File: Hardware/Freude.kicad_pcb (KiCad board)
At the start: 4 copper layers, 10 parts, among them U1 IQS572

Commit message: Add uc, inter connects, futter to schematic
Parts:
- added REF**: Touchpad, Custom_Touchpad:Touchpad, B.Cu at (199.5, 75.8)
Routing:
- net (no net): track 0.00 -> 4.75 mm, vias 0 -> 1

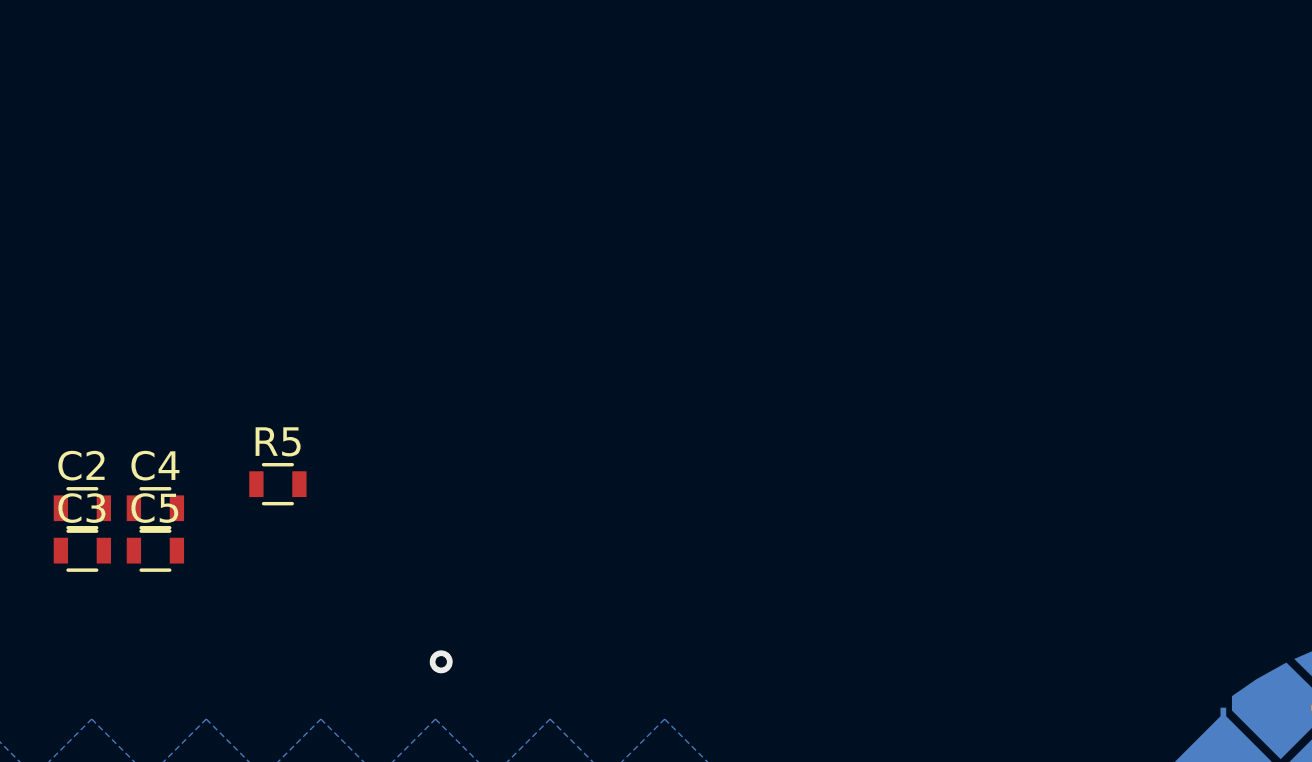
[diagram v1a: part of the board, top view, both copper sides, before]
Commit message: added 5 pin connector, added envelope for uc board, changed uc to low power smaller footprint after seeing envelope
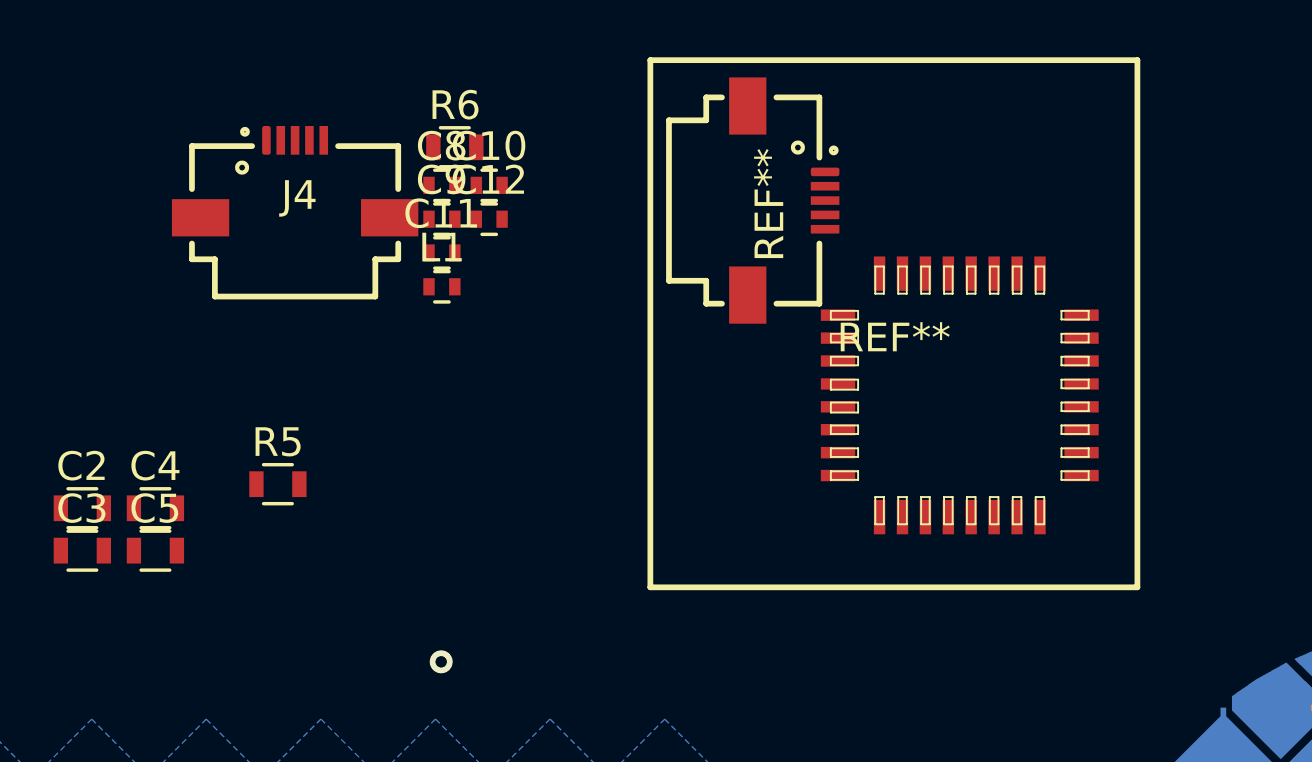
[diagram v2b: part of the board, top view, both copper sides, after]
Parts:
- added >NAME: >VALUE, SparkFun-DigitalIC:LQFP-32, F.Cu at (182.3, 54.9)
- added C10: 100pF, Resistors_SMD:R_0402, F.Cu at (165.9, 47.6)
- added C11: 100pF, Resistors_SMD:R_0402, F.Cu at (164.2, 49.9)
- added C12: 1uF, Resistors_SMD:R_0402, F.Cu at (165.9, 48.8)
- added C8: 100pF, Resistors_SMD:R_0402, F.Cu at (164.2, 47.6)
- added C9: 1uF, Resistors_SMD:R_0402, F.Cu at (164.2, 48.8)
- added J4: Conn_01x05_Female, .pretty:5051100592, F.Cu at (159.1, 46.0)
- added L1: Ferrite_Bead_Small, Resistors_SMD:R_0402, F.Cu at (164.2, 51.1)
- added R6: 0, Resistors_SMD:R_0603, F.Cu at (164.7, 46.2)
- added REF**: Joystick Envelope, .pretty:Joystick Envelope, F.Cu at (180.0, 52.4)
- added REF**: 5051100592, .pretty:5051100592, F.Cu at (177.6, 48.1)
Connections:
- net +3V3 renamed +3.3VA
- net /RDY renamed /RDY_TP
- net /SCL renamed /SCL_TP
- net /SDA renamed /SDA_TP
- C2 pad 1: Net-(C2-Pad1) -> GNDA
- C3 pad 1: Net-(C2-Pad1) -> GNDA
- C4 pad 1: Net-(C2-Pad1) -> GNDA
- C5 pad 1: Net-(C2-Pad1) -> GNDA
- R3 pad 2: GND -> GNDA
- R4 pad 2: GND -> GNDA
- R5 pad 2: GND -> GNDA
- U1 pad 5: GND -> GNDA

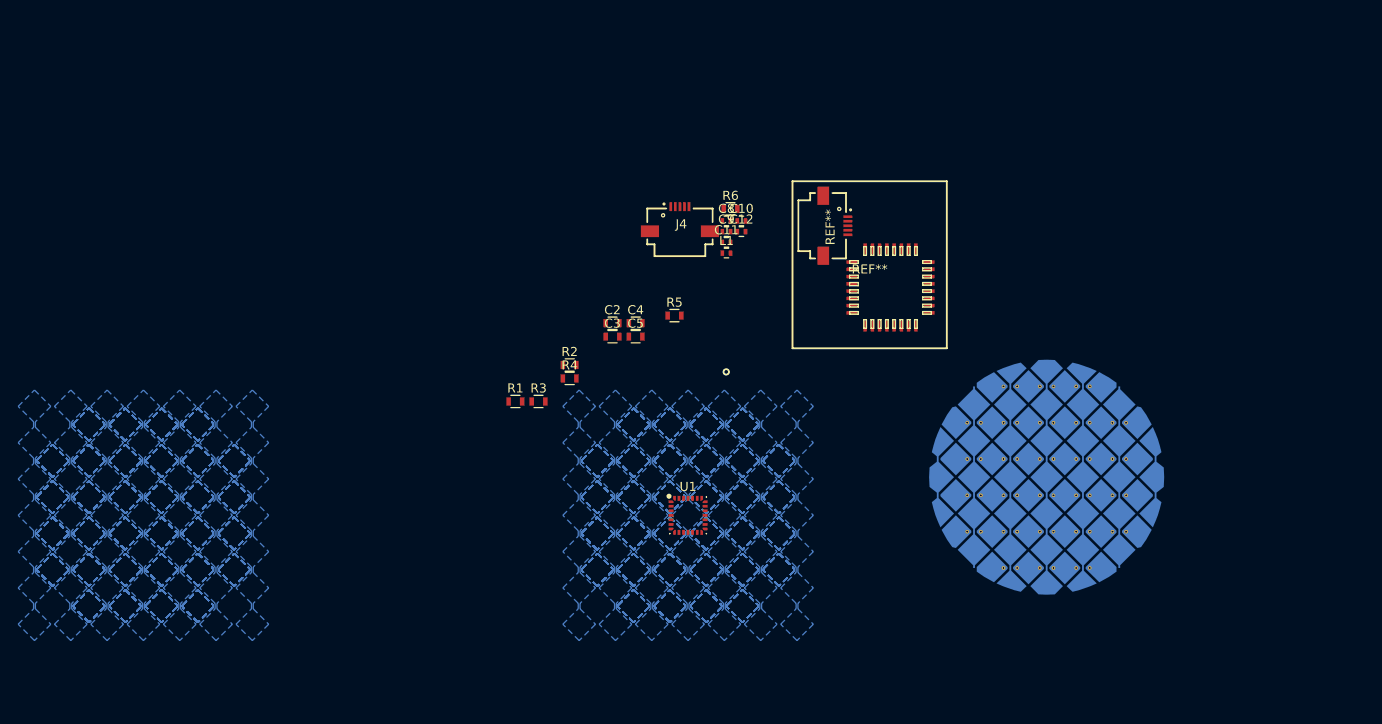
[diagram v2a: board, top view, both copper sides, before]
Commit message: add connectors, symbol for touch pad, start placement of touch controller
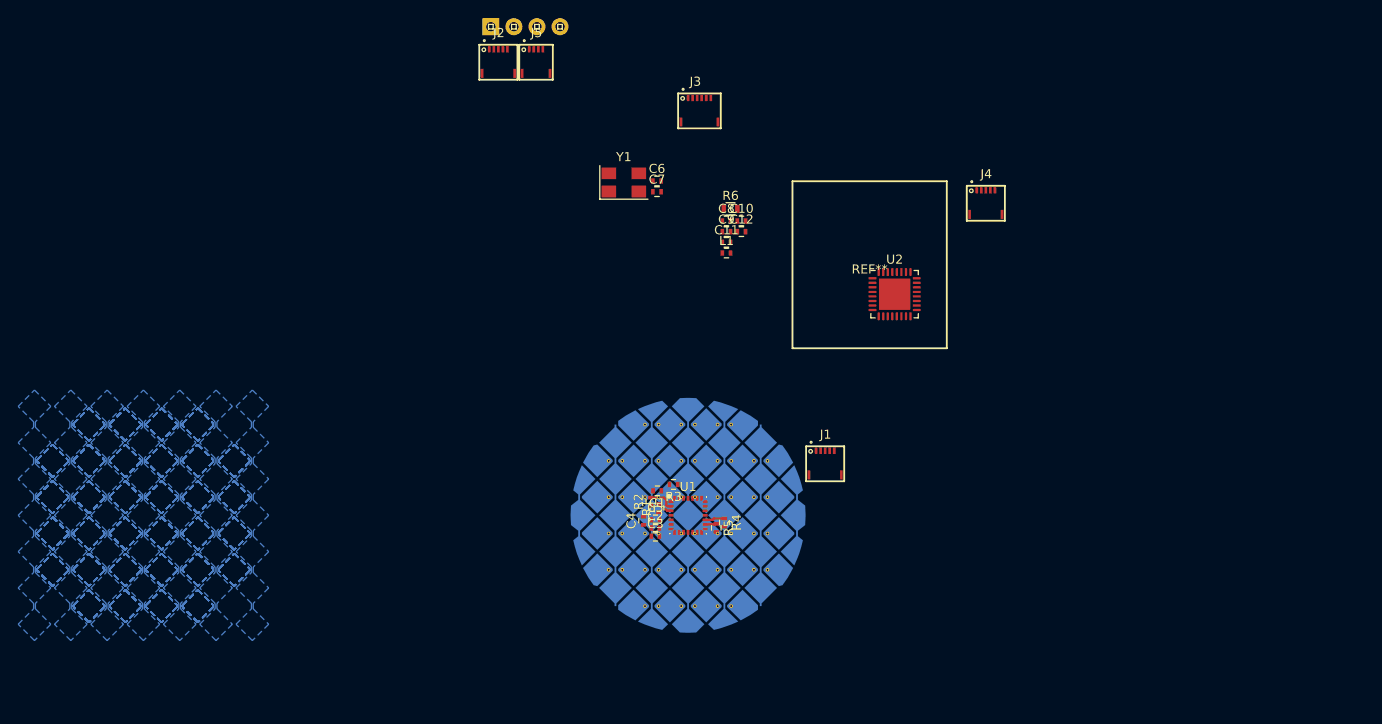
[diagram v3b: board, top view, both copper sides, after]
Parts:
- removed >NAME: >VALUE, SparkFun-DigitalIC:LQFP-32
- removed the REF** at (177.6, 48.1)
- added C1: C_Small, Resistors_SMD:R_0402, F.Cu at (156.6, 77.3)
- added C6: 30pF, Resistors_SMD:R_0402, F.Cu at (156.6, 43.2)
- added C7: 30pF, Resistors_SMD:R_0402, F.Cu at (156.6, 44.4)
- added J1: Conn_01x05_Female, .pretty:503480-0500, F.Cu at (175.1, 72.9)
- added J2: Conn_01x05_Female, .pretty:503480-0500, F.Cu at (139.1, 28.7)
- added J3: Conn_01x06_Female, .pretty:503480-0600, F.Cu at (161.3, 34.0)
- added J5: Conn_01x04_Female, .pretty:503480-0400, F.Cu at (143.3, 28.7)
- added J6: Conn_01x04_Male, SparkFun-Connectors:1X04, F.Cu at (138.3, 26.2)
- added U2: STM32L432KBUx, Package_DFN_QFN:QFN-32-1EP_5x5mm_P0.5mm_EP3.45x3.45mm, F.Cu at (182.8, 55.6)
- added Y1: Crystal_GND24, Crystal_SMD_5032-4pin_5.0x3.2mm, F.Cu at (152.9, 43.3)
- C2, C3, C4, C5, R1, R2, R3, R4, R5: footprint Resistors_SMD:R_0603 -> Resistors_SMD:R_0402
- J4: value Conn_01x05_Female -> Conn_01x04_Female; footprint .pretty:5051100592 -> .pretty:503480-0500
- moved REF** 39.7 mm to (160.0, 80.0)
- moved J4 33.7 mm to (192.8, 44.2)
- moved R5 23.8 mm to (163.1, 81.4), turned to 270 degrees
- moved R4 23.3 mm to (164.0, 80.8), turned to 270 degrees
- moved C2 23.0 mm to (156.4, 81.4)
- moved C3 22.5 mm to (156.4, 82.3)
- moved C4 21.8 mm to (155.1, 80.6), turned to 90 degrees
- moved C5 20.3 mm to (156.4, 80.5)
- moved R1 19.7 mm to (156.8, 79.2), turned to 90 degrees
- moved R2 17.5 mm to (155.9, 78.5), turned to 90 degrees
- moved R3 17.5 mm to (158.4, 76.6), turned to 180 degrees
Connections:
- J4 pad 2: GND -> /SWDIO
- J4 pad 3: /Switch_Out -> /SWCLK
- J4 pad 4: /DAC2_OUT1 -> GND
- J4 pad 5: +3V3 -> (no net)
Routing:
- net /SDA_TP: track 0.00 -> 2.67 mm
- net Net-(R4-Pad1): track 0.00 -> 2.19 mm
- net Net-(R5-Pad1): track 0.00 -> 1.25 mm
- net /SCL_TP: track 0.00 -> 0.71 mm
- net (no net): vias 1 -> 0

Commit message: Route touchpad complete *airhorn*, add switch schematic, add domain boxes schematic
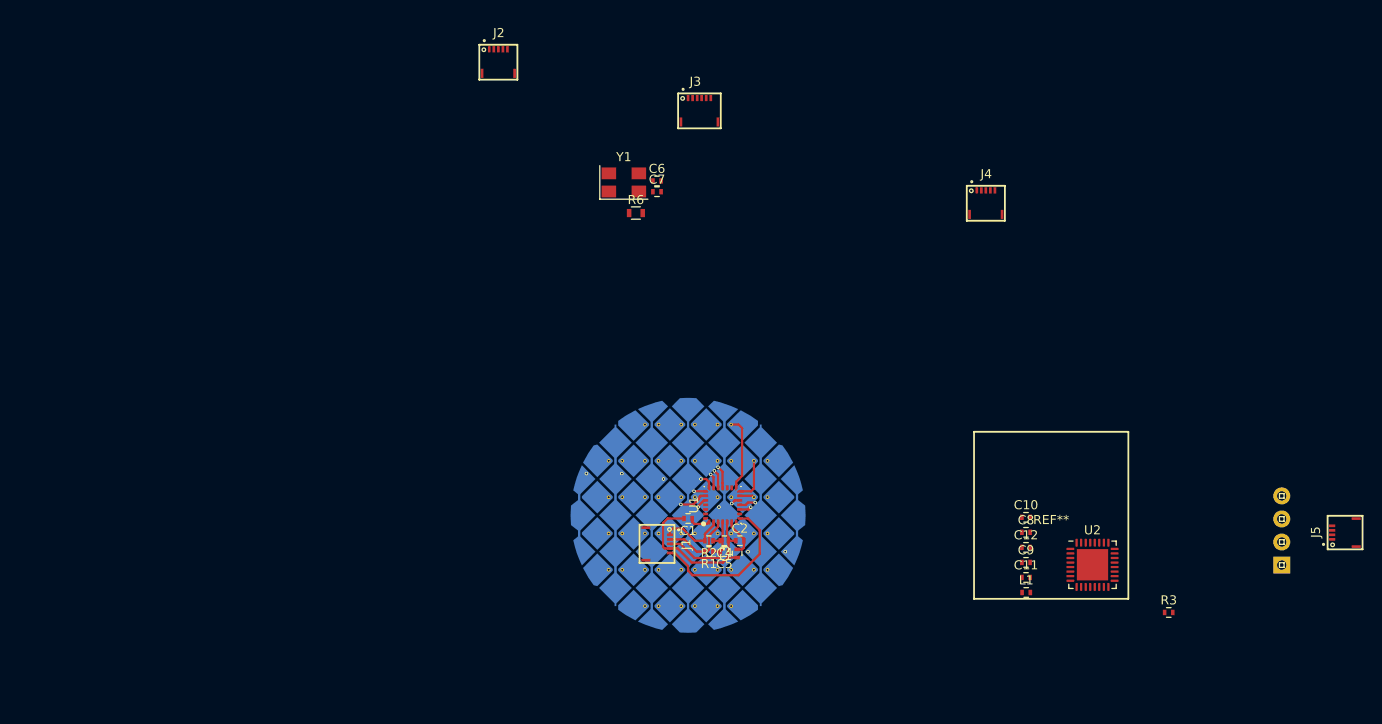
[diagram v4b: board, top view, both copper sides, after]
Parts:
- removed R4, R5: 0, Resistors_SMD:R_0402
- removed the REF** at (160.0, 80.0)
- added X1: Custom_Touchpad, Custom_Touchpad:Touchpad, B.Cu at (160.0, 80.0)
- R3: value 0 -> 10k
- moved J6 105.4 mm to (225.4, 85.5), turned to 90 degrees
- moved J5 102.6 mm to (230.9, 81.9), turned to 90 degrees
- moved R3 56.3 mm to (212.9, 90.7), turned to 0 degrees
- moved L1 49.9 mm to (197.2, 88.5)
- moved C11 49.5 mm to (197.2, 86.8)
- moved C9 49.2 mm to (197.2, 85.2)
- moved C8 47.6 mm to (197.2, 81.9)
- moved C12 46.8 mm to (197.2, 83.5)
- moved C10 45.3 mm to (197.2, 80.2)
- moved U2 36.9 mm to (204.6, 85.5)
- moved REF** 34.1 mm to (200.0, 80.0)
- moved J1 19.9 mm to (158.0, 83.2), turned to 270 degrees
- moved R6 10.4 mm to (154.2, 46.7)
- moved C2 9.40 mm to (165.7, 82.8)
- moved C3 9.20 mm to (165.4, 84.2), turned to 90 degrees
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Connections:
- net /VCC renamed /Prog_VCC
- net XA07 renamed Net-(U1-Pad25)
- J1 pad 1: +3.3VA -> /SDA_TP
- J1 pad 2: /SDA_TP -> /SCL_TP
- J1 pad 3: /SCL_TP -> +3.3VA
- J1 pad 4: /RDY_TP -> GNDA
- J1 pad 5: GNDA -> /RDY_TP
- J3 pad 1: +3V3 -> /SDA_UC
- J3 pad 2: /SDA_UC -> /SCL_UC
- J3 pad 3: /SCL_UC -> +3V3
- J3 pad 4: /RDY_UC -> GND
- J3 pad 5: GND -> /RDY_UC
- J5 pad 2: /SWDIO -> /Prog_SWDIO
- J5 pad 3: /SWCLK -> /Prog_SWCLK
- J5 pad 4: GND -> /Prog_GND
- J6 pad 2: /SWDIO -> /Prog_SWDIO
- J6 pad 3: /SWCLK -> /Prog_SWCLK
- J6 pad 4: GND -> /Prog_GND
- R3 pad 1: Net-(R3-Pad1) -> +3V3
- R3 pad 2: GNDA -> /Switch_In
- U1 pad 26: Net-(R3-Pad1) -> Net-(U1-Pad26)
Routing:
- net XA02: track 0.00 -> 31.0 mm, vias 0 -> 2
- net XA05: track 0.00 -> 30.2 mm, vias 0 -> 2
- net XA04: track 0.00 -> 29.2 mm, vias 0 -> 2
- net XA01: track 0.00 -> 28.4 mm, vias 0 -> 2
- net XA03: track 0.00 -> 25.7 mm, vias 0 -> 1
- net XA00: track 0.00 -> 25.3 mm, vias 0 -> 2
- net XA06: track 0.00 -> 22.3 mm, vias 0 -> 2
- net GNDA: track 0.00 -> 19.1 mm
- net YA01: track 0.00 -> 18.0 mm, vias 0 -> 1
- net YA00: track 0.00 -> 18.0 mm, vias 0 -> 1
- net /RDY_TP: track 0.00 -> 17.5 mm
- net YA05: track 0.00 -> 12.7 mm
- net YA04: track 0.00 -> 12.2 mm
- net +3.3VA: track 0.00 -> 12.0 mm
- net YA02: track 0.00 -> 11.7 mm, vias 0 -> 1
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- removed copper zone on B.Cu, net (none)
- removed copper zone on B.Cu, net Net-(U1-Pad25)
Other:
- net class Default: via_dia 0.8 -> 0.4; via_drill 0.4 -> 0.2
- rule via_min_drill: 0.3 -> 0.2

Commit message: fix several power connection errors on U2 -power and ground, perhaps- added 6-pin connector to touch pad to match brain board after rejecting 180 deg connector
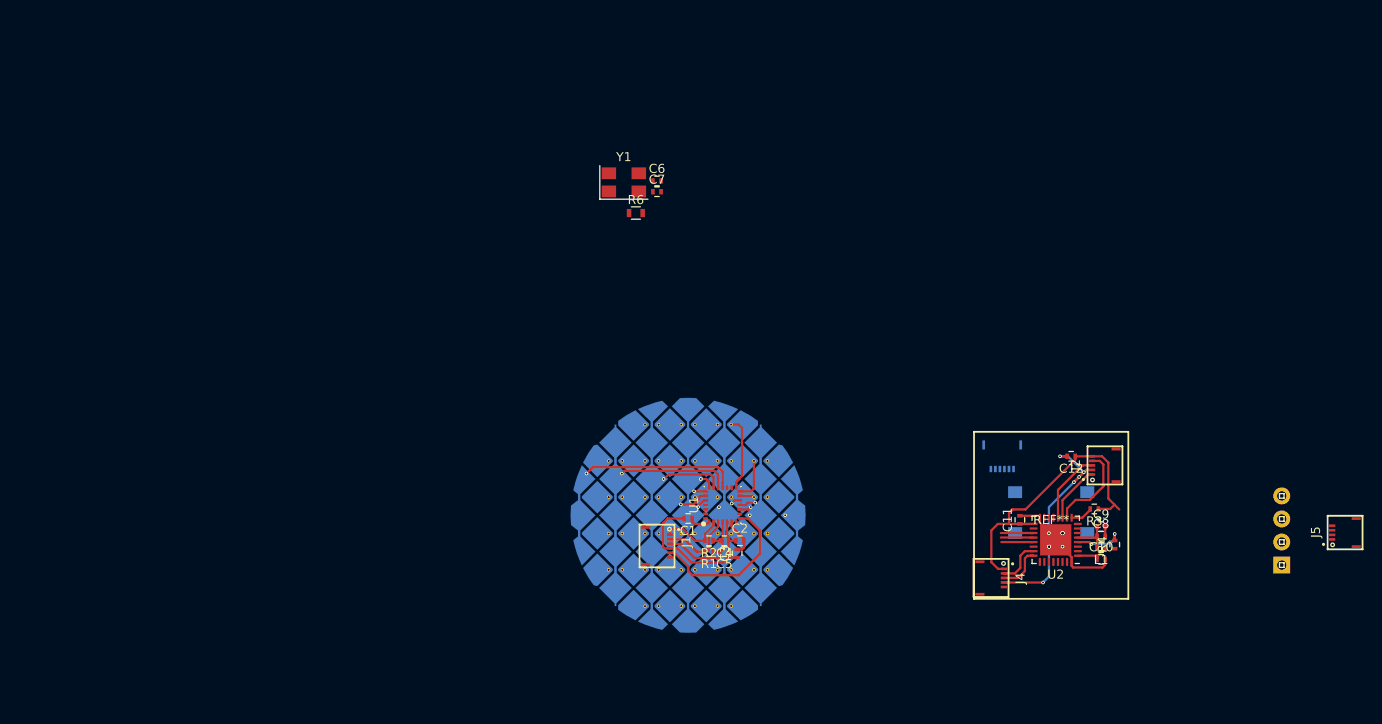
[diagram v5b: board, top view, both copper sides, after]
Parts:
- added R4: 10k, Resistors_SMD:R_0402, F.Cu at (207.0, 83.2)
- added REF**: Switch_Tactile_SMD_6x6mm_PTS645, digikey-footprints:Switch_Tactile_SMD_6x6mm_PTS645, B.Cu at (200.0, 79.7)
- J1: value Conn_01x05_Female -> Conn_01x06_Female; footprint .pretty:503480-0500 -> .pretty:503480-0600
- J3: moved to B.Cu
- moved J2 79.9 mm to (204.5, 74.5), turned to 90 degrees
- moved J3 52.8 mm to (194.6, 74.9)
- moved J4 42.7 mm to (194.8, 86.9), turned to 270 degrees
- moved R3 14.0 mm to (204.8, 79.3), turned to 180 degrees
- moved C12 11.2 mm to (202.2, 73.5), turned to 180 degrees
- moved L1 9.62 mm to (205.5, 83.5), turned to 180 degrees
- moved C10 9.48 mm to (205.5, 84.8)
- moved C9 9.16 mm to (205.5, 81.2)
- moved C8 8.29 mm to (205.5, 82.3)
- moved C11 6.38 mm to (196.6, 80.5), turned to 90 degrees
- moved U2 4.90 mm to (200.5, 82.7), turned to 180 degrees
- moved J1 0.22 mm to (158.0, 83.4)
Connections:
- C10 pad 1: Net-(C10-Pad1) -> +3V3
- C10 pad 2: Net-(C10-Pad2) -> GND
- C11 pad 1: Net-(C10-Pad1) -> +3V3
- C11 pad 2: Net-(C10-Pad2) -> GND
- C12 pad 1: Net-(C10-Pad1) -> +3V3
- C12 pad 2: Net-(C10-Pad2) -> GND
- C8 pad 2: Net-(C10-Pad2) -> GND
- C9 pad 2: Net-(C10-Pad2) -> GND
- J2 pad 1: /DAC1_OUT2 -> /DAC2_OUT1
- J2 pad 4: /DAC2_OUT1 -> /DAC1_OUT2
- J3 pad 6: Net-(J3-Pad6) -> /AZO_UNK
- L1 pad 1: Net-(C10-Pad1) -> +3V3
- U2 pad 1: Net-(C10-Pad1) -> +3V3
- U2 pad 16: Net-(U2-Pad16) -> GND
- U2 pad 17: Net-(C10-Pad1) -> +3V3
- U2 pad 22: Net-(U2-Pad22) -> /AZO_UNK
- U2 pad 32: Net-(U2-Pad32) -> GND
- U2 pad 33: Net-(U2-Pad33) -> GND
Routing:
- net GND: track 0.00 -> 39.7 mm, vias 0 -> 15
- net +3V3: track 0.00 -> 36.9 mm
- net /DAC1_OUT2: track 0.00 -> 9.84 mm
- net /Switch_Out: track 0.00 -> 8.43 mm
- net /DAC2_OUT1: track 0.00 -> 6.36 mm
- net Net-(R4-Pad2): track 0.00 -> 5.68 mm, vias 0 -> 2
- net /SWCLK: track 0.00 -> 5.46 mm
- net /SWDIO: track 0.00 -> 5.27 mm
- net Net-(C8-Pad1): track 0.00 -> 4.47 mm
- net /SDA_UC: track 0.00 -> 3.61 mm
- net /SCL_UC: track 0.00 -> 3.61 mm
- net /RDY_UC: track 0.00 -> 3.56 mm
- net XA06: track 22.3 -> 19.1 mm
- net XA05: track 30.2 -> 27.3 mm
- net /Switch_In: track 0.00 -> 2.51 mm
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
